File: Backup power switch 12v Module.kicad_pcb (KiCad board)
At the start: 2 copper layers, 94.3 x 76.2 mm, 58 parts, among them J1 BAT/PWR IN, J2 External, J3 PWR OUT, J4 Barrel_Jack_MountingPin, J5 Esternal, J6 Barrel_Jack_MountingPin, J7 Barrel_Jack_MountingPin, J8 Barrel_Jack_MountingPin, J9 PWR SELECTOR, K1 SRD-12VDC-SL-C, Q2 AO3401A, Q3 BSS138, U2 INA219AxD, U3 INA219AxD, U4 LTV-817, U5 LTV-817, U6 CN3763, U7 ESP32-C3 Pro Mini, U8 AMS1117-3.3

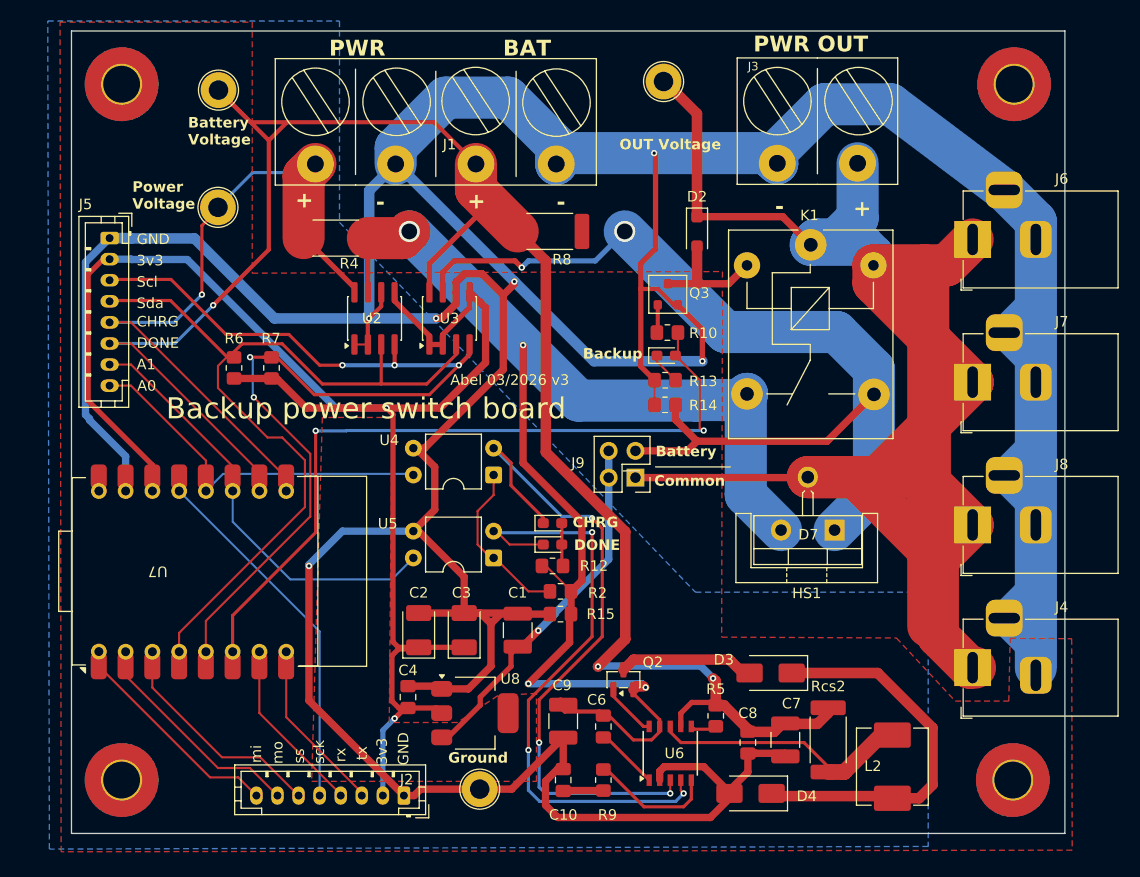
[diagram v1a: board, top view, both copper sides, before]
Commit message: Add more space aroung relay
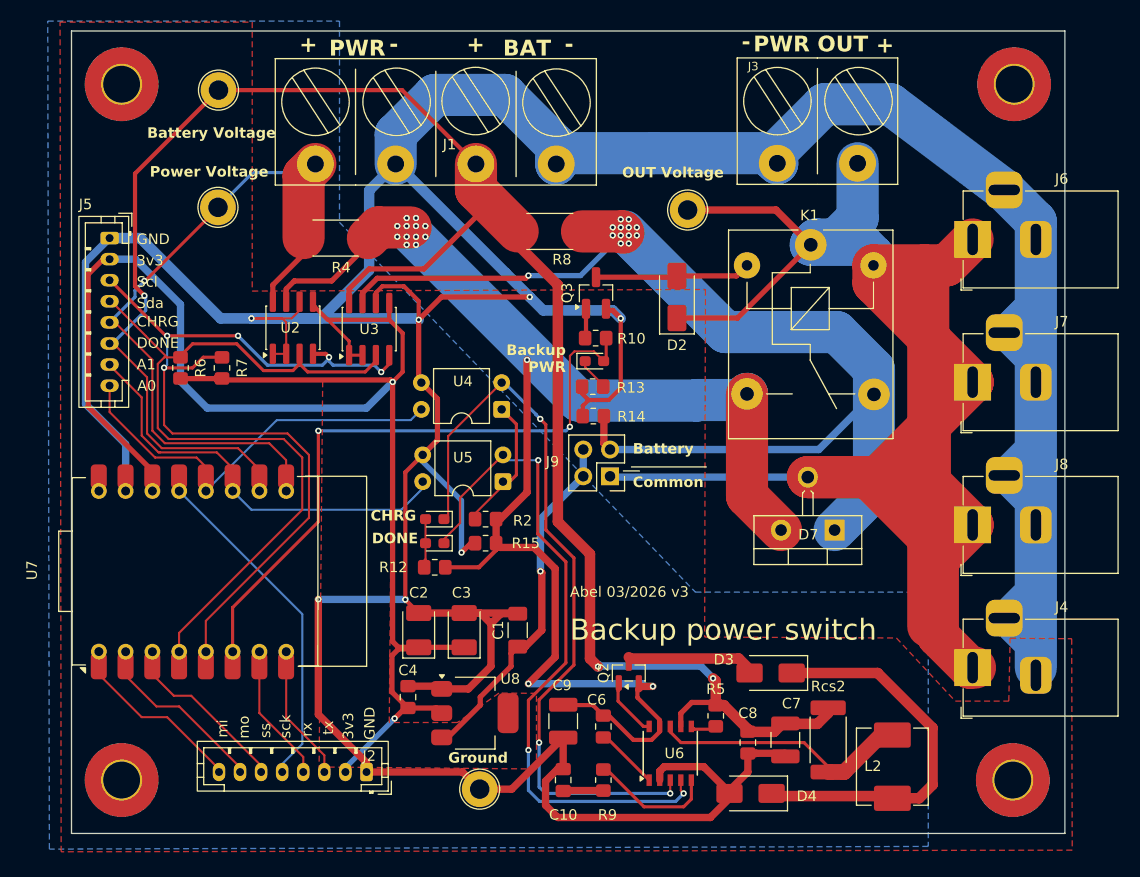
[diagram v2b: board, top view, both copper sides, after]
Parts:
- removed HS1: Heatsink, Heatsink:Heatsink_Stonecold_HS-S01_13.21x6.35mm
- C1: footprint Capacitor_SMD:C_1210_3225Metric_Pad1.33x2.70mm_HandSolder -> Capacitor_SMD:C_1206_3216Metric_Pad1.33x1.80mm_HandSolder
- D2: footprint Diode_SMD:D_SOD-123F -> Diode_SMD:D_SMA
- Q3: footprint PCM_Package_TO_SOT_SMD_AKL:SOT-23 -> Package_TO_SOT_SMD:SOT-23_Handsoldering
- moved TP4 12.4 mm to (147.7, 75.4)
- moved D5 11.2 mm to (123.7, 104.8), turned to 180 degrees
- moved D1 11.2 mm to (123.7, 107.1), turned to 180 degrees
- moved R12 11.2 mm to (123.7, 109.3), turned to 0 degrees
- moved R2 9.88 mm to (128.5, 104.8)
- moved R15 9.79 mm to (128.5, 107.1)
- moved U2 7.80 mm to (110.2, 86.6)
- moved U3 7.69 mm to (117.5, 86.7)
- moved U5 7.29 mm to (130.2, 101.2)
- moved R13 6.90 mm to (138.7, 92.2)
- moved R14 6.89 mm to (138.8, 95.0)
- moved D6 6.83 mm to (138.9, 89.8)
- moved R10 6.83 mm to (139.0, 87.6)
- moved Q3 6.81 mm to (139.0, 83.3)
- moved D2 6.51 mm to (146.7, 83.7), turned to 90 degrees
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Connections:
- U8 pad 2: +3V3 -> unconnected-(U8-Heat-Pad4)
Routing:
- net GNDPWR: track 507.5 -> 492.8 mm, vias 6 -> 7
- net SCL: track 99.1 -> 87.6 mm
- net SIG: track 73.0 -> 62.5 mm
- net /PWR OUT 12 +: track 131.7 -> 141.8 mm, vias 4 -> 15
- net /Li-Io 3S Batary Charger module/CHRG: track 63.7 -> 71.9 mm
- net BAT OUT 12 +: track 100.7 -> 108.8 mm, vias 2 -> 13
- net /Li-Io 3S Batary Charger module/DONE: track 58.6 -> 65.4 mm
- net COMMON OUT 12 +: track 195.3 -> 201.0 mm
- net SS: track 20.2 -> 15.3 mm
- net SDA: track 83.0 -> 78.5 mm
- net CHRG_SIG: track 35.4 -> 39.8 mm
- net MOSI: track 20.0 -> 15.8 mm
- net MISO: track 20.0 -> 16.2 mm
- net TTL-TX: track 15.3 -> 11.6 mm
- net TTL-RX: track 15.5 -> 11.8 mm
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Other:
- board text added: "Backup PWR"
- board text added: "Backup power switch"
- board text removed: "Backup"
- board text removed: "Backup power switch board"

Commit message: Add holes for alt diodes. Prod. Docs
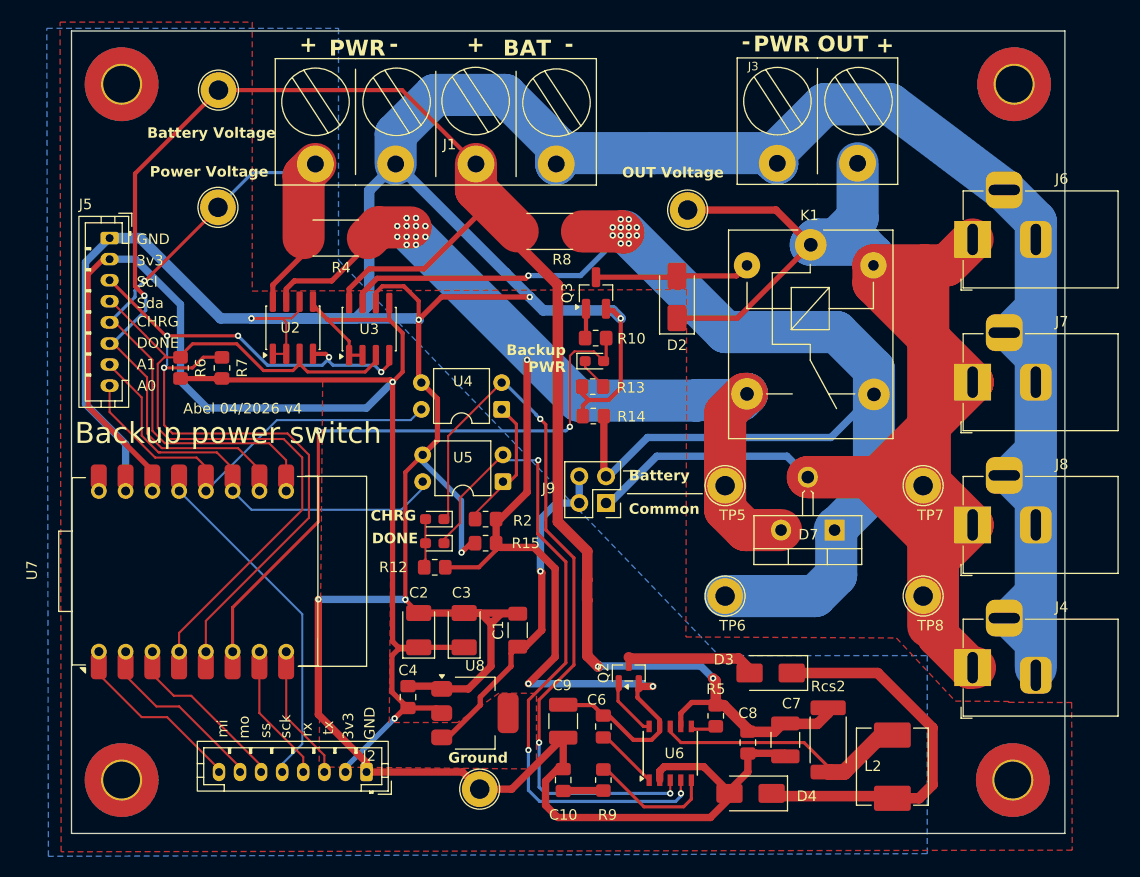
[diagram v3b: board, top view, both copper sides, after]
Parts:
- added TP5: OUT, TestPoint:TestPoint_Loop_D2.50mm_Drill1.85mm, F.Cu at (151.3, 101.6)
- added TP6: OUT, TestPoint:TestPoint_Loop_D2.50mm_Drill1.85mm, F.Cu at (151.3, 112.1)
- added TP7: OUT, TestPoint:TestPoint_Loop_D2.50mm_Drill1.85mm, F.Cu at (170.1, 101.6)
- added TP8: OUT, TestPoint:TestPoint_Loop_D2.50mm_Drill1.85mm, F.Cu at (170.1, 112.1)
- U8: footprint Package_TO_SOT_SMD:SOT-223-3_TabPin2 -> Package_TO_SOT_SMD:SOT-223
- moved J9 2.57 mm to (140.0, 103.3)
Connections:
- D7 pad 1: BAT OUT 12 + -> unconnected-(D7-A1-Pad1)
- U8 pad 2: unconnected-(U8-Heat-Pad4) -> +3V3
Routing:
- net BAT OUT 12 +: track 108.8 -> 128.5 mm
- net /PWR OUT 12 +: track 141.8 -> 145.6 mm
- net COMMON OUT 12 +: track 201.0 -> 204.0 mm
- net GNDPWR: track 492.8 -> 494.7 mm
- net Net-(J9-Pin_2): track 33.8 -> 32.3 mm
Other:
- board text added: "Abel 04/2026 v4"
- board text removed: "Abel 03/2026 v3"

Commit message: add info
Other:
- board text added: "Alt D7"
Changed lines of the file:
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@@
 		)
 		(embedded_fonts no)
-		(model "TO-220-3_Staggered_Vertical"
+		(model "${KICAD10_3DMODEL_DIR}/Package_TO_SOT_THT.3dshapes/TO-220-3_Vertical.step"
 			(offset
 				(xyz 0 0 0)
@@
 		)
 	)
+	(gr_poly
+		(pts
+			(xy 156.63114 97.231332) (xy 156.63114 100.787332) (xy 159.67914 99.009332)
+		)
+		(stroke
+			(width 0.1)
+			(type solid)
+		)
+		(fill yes)
+		(layer "F.SilkS")
+	)
+	(gr_poly
+		(pts
+			(xy 157.099 110.363) (xy 157.099 113.919) (xy 160.147 112.141)
+		)
+		(stroke
+			(width 0.1)
+			(type solid)
+		)
+		(fill yes)
+		(layer "F.SilkS")
+	)
 	(gr_line
 		(start 141.986 102.362)
@@
 		(layer "F.SilkS")
 	)
+	(gr_line
+		(start 153.162 99.06)
+		(end 167.005 99.009332)
+		(stroke
+			(width 0.1)
+			(type default)
+		)
+		(layer "F.SilkS")
+	)
+	(gr_line
+		(start 153.797 112.141)
+		(end 167.513 112.141)
+		(stroke
+			(width 0.1)
+			(type default)
+		)
+		(layer "F.SilkS")
+	)
+	(gr_rect
+		(start 159.67914 97.294832)
+		(end 159.93314 100.723832)
+		(stroke
+			(width 0.1)
+			(type solid)
+		)
+		(fill yes)
+		(layer "F.SilkS")
+	)
+	(gr_rect
+		(start 160.147 110.4265)
+		(end 160.401 113.8555)
+		(stroke
+			(width 0.1)
+			(type solid)
+		)
+		(fill yes)
+		(layer "F.SilkS")
+	)
 	(gr_rect
 		(start 89.2212 58.445886)
@@
 		)
 	)
+	(gr_text "Alt D7"
+		(at 161.29 111.76 0)
+		(layer "F.SilkS")
+		(effects
+			(font
+				(size 1 1)
+				(thickness 0.15)
+			)
+			(justify left bottom)
+		)
+	)
+	(gr_text "Alt D7"
+		(at 161.417 100.33 0)
+		(layer "F.SilkS")
+		(effects
+			(font
+				(size 1 1)
+				(thickness 0.15)
+			)
+			(justify left bottom)
+		)
+	)
 	(gr_text "mi"
 		(at 104.14 125.508907 90)
@@
 		)
 	)
+	(group ""
+		(members "355335cb-b251-431e-87b0-449b19cecf26" "b791b449-b0e7-44aa-a014-3322d08df297"
+			"e0c4e784-15b2-4203-a9ff-8d198c87ffbe"
+		)
+	)
